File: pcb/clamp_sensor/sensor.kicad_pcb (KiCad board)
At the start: 2 copper layers, 45 x 36 mm, 7 parts, among them J1 Conn_01x08

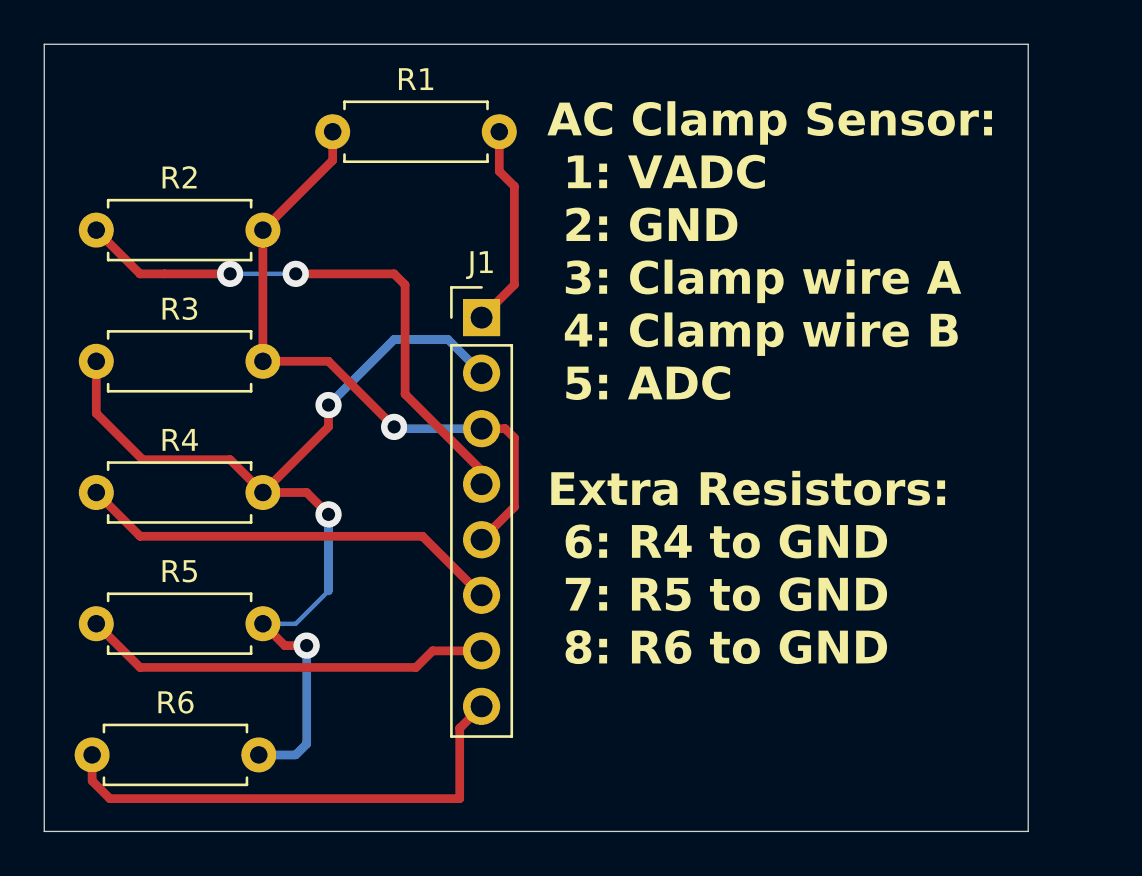
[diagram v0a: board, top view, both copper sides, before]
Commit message: PCB: Clamp sensor update
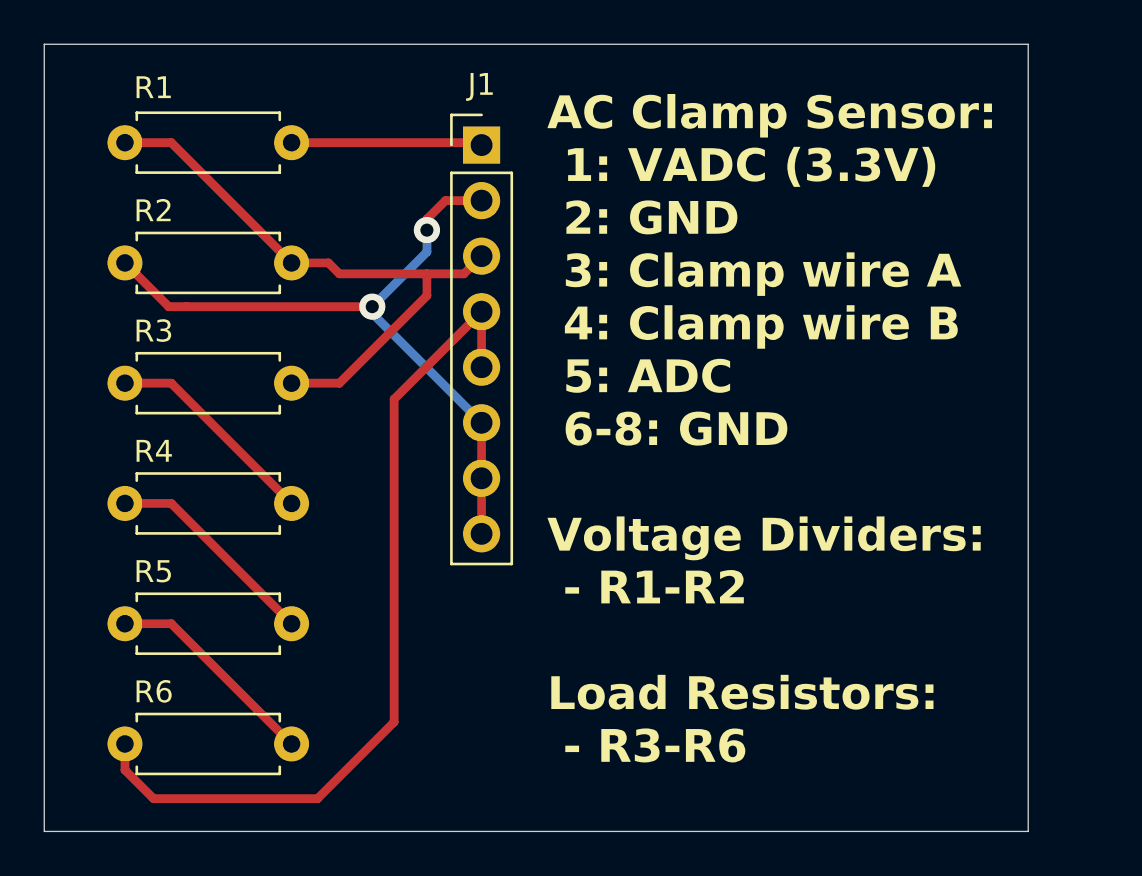
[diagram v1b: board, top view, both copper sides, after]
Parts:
- moved R1 9.51 mm to (52.2, 39.5)
- moved J1 7.89 mm to (68.5, 39.6)
- moved R2 1.99 mm to (52.2, 45.0)
- moved R3 1.65 mm to (52.2, 50.5)
- moved R6 1.58 mm to (52.2, 67.0)
- moved R4 1.40 mm to (52.2, 56.0)
- moved R5 1.31 mm to (52.2, 61.5)
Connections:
- J1 pad 5: Net-(J1-Pin_3) -> Net-(J1-Pin_4)
- J1 pad 6: Net-(J1-Pin_6) -> Net-(J1-Pin_2)
- J1 pad 7: Net-(J1-Pin_7) -> Net-(J1-Pin_2)
- J1 pad 8: Net-(J1-Pin_8) -> Net-(J1-Pin_2)
- R2 pad 1: Net-(J1-Pin_4) -> Net-(J1-Pin_2)
- R3 pad 1: Net-(J1-Pin_2) -> Net-(R3-Pad1)
- R4 pad 1: Net-(J1-Pin_6) -> Net-(R4-Pad1)
- R4 pad 2: Net-(J1-Pin_2) -> Net-(R3-Pad1)
- R5 pad 1: Net-(J1-Pin_7) -> Net-(R5-Pad1)
- R5 pad 2: Net-(J1-Pin_2) -> Net-(R4-Pad1)
- R6 pad 1: Net-(J1-Pin_8) -> Net-(J1-Pin_4)
- R6 pad 2: Net-(J1-Pin_2) -> Net-(R5-Pad1)
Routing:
- net Net-(J1-Pin_8): track 23.0 -> 0.00 mm
- net Net-(J1-Pin_6): track 19.6 -> 0.00 mm
- net Net-(J1-Pin_7): track 18.8 -> 0.00 mm
- net Net-(J1-Pin_2): track 45.5 -> 32.5 mm, vias 3 -> 2
- net Net-(J1-Pin_4): track 25.7 -> 38.5 mm, vias 2 -> 0
- net Net-(R5-Pad1): track 0.00 -> 9.90 mm
- net Net-(R4-Pad1): track 0.00 -> 9.90 mm
- net Net-(R3-Pad1): track 0.00 -> 9.90 mm
- net Net-(J1-Pin_3): track 30.1 -> 28.0 mm, vias 1 -> 0
- net Net-(J1-Pin_1): track 9.41 -> 8.74 mm
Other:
- board text added: "AC Clamp Sensor: 1: VADC (3.3V) 2: GND 3: Clamp wire A 4: Clamp wire B 5: ADC 6-8: GND Voltage Dividers: - R1-R2 Load Resistors: - R3-R6"
- board text removed: "AC Clamp Sensor: 1: VADC 2: GND 3: Clamp wire A 4: Clamp wire B 5: ADC Extra Resistors: 6: R4 to GND 7: R5 to GND 8: R6 to GND"
